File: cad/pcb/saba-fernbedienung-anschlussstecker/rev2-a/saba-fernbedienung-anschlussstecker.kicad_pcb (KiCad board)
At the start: 2 copper layers, 38.5 x 39.1 mm, 8 parts, among them J101 Conn_01x04, J102 Conn_01x04, J103 Conn_01x04, J104 Conn_01x02, J105 Conn_01x04, J106 Conn_01x04, X101 Stecker-6-3D

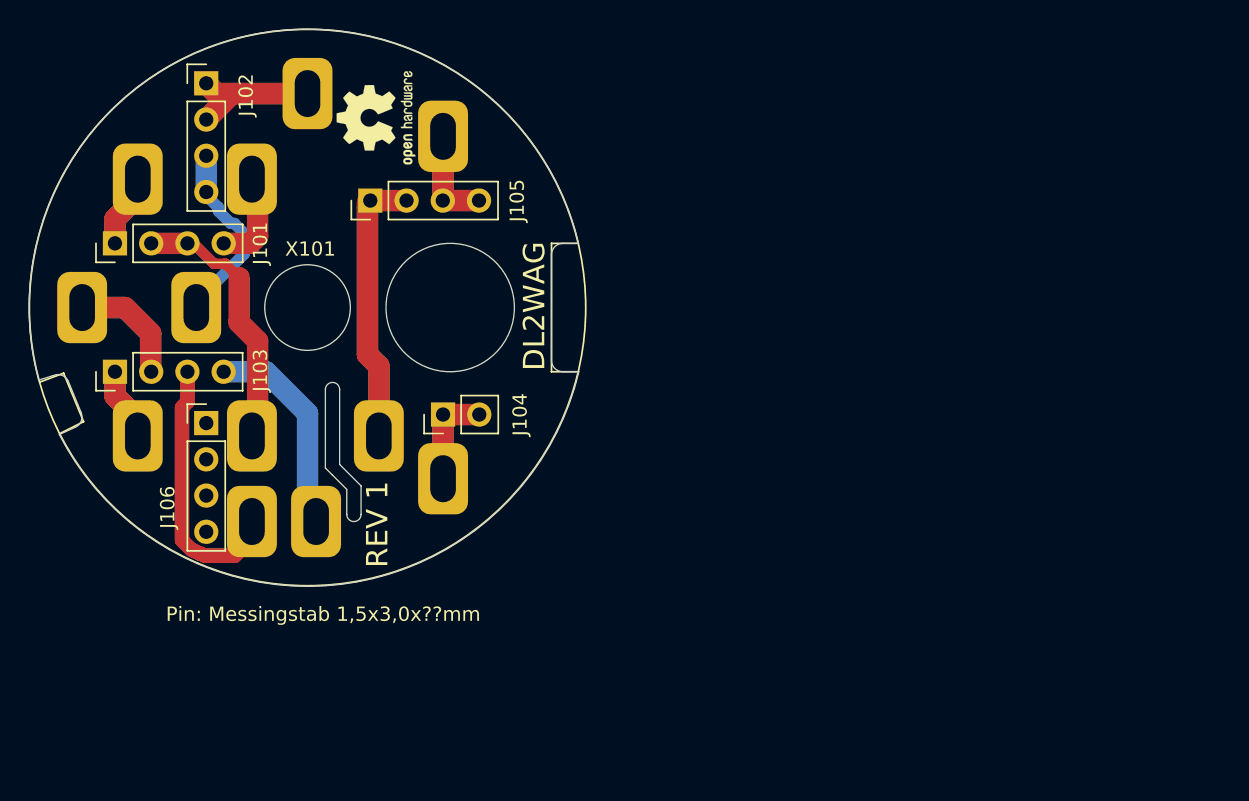
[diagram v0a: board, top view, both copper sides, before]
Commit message: Fix: Stecker
- Durchmesser Mittelloch groesser
- Position Befestigungsloch weiter rechts
- Position Pin15 korrigiert
- Pin11 hinzugefuegt. Ist in der Steckdose nicht belegt.
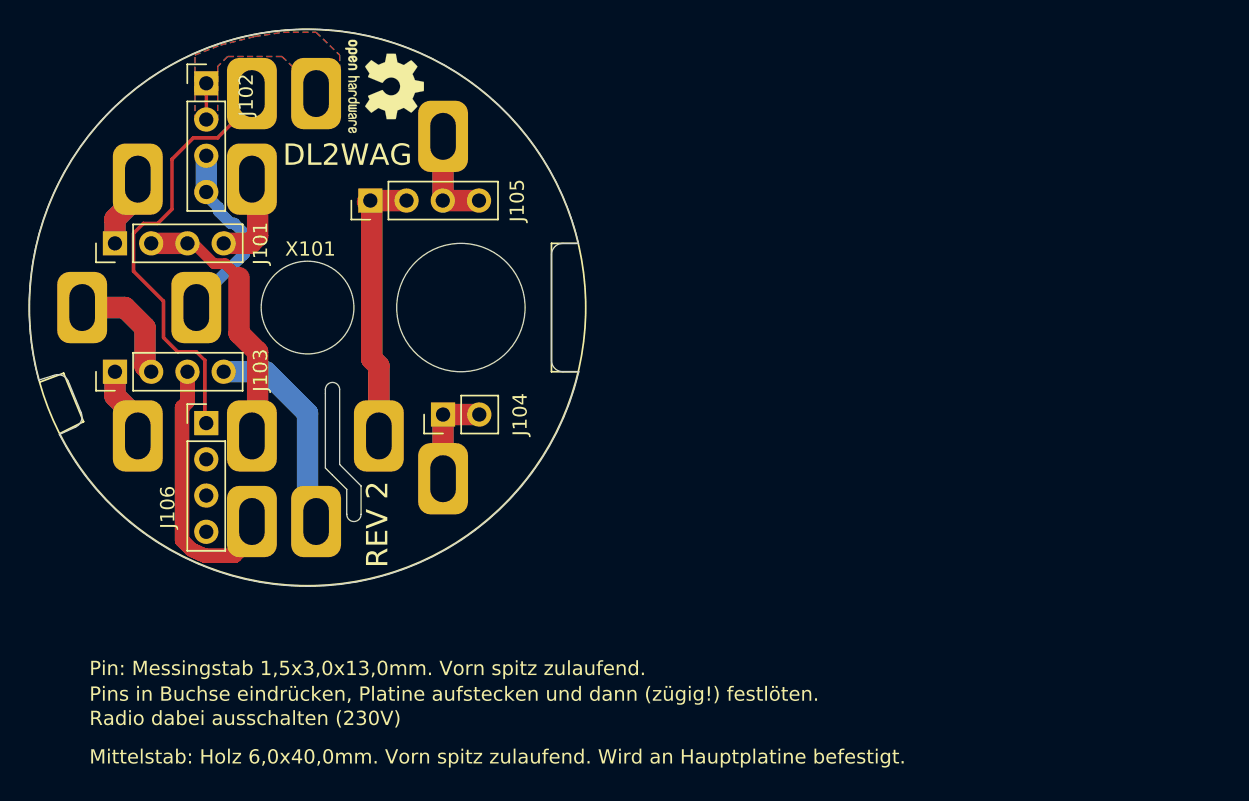
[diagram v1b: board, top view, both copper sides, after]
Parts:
- added ?: , , F.Cu at (-14.4, 40.9)
- added ?: , , F.Cu at (-16.3, 40.0)
- added ?: , , F.Cu at (-13.8, 35.7)
- moved REF** 2.28 mm to (135.4, 64.5), turned to 270 degrees
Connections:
- J106 pad 1: (no net) -> Net-(J106-Pad1)
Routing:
- net Net-(J106-Pad1): track 0.00 -> 31.2 mm
- net Net-(J102-Pad1): track 18.1 -> 2.52 mm
- added copper zone on B.Cu, net Net-(J102-Pad1)
- added copper zone on F.Cu, net Net-(J102-Pad1)
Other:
- board text added: "REV 2"
- board text removed: "REV 1"
